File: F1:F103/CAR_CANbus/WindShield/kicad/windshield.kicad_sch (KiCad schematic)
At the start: 48 parts, among them J1 Screw_Terminal_01x02, J2 Screw_Terminal_01x02, J3 Screw_Terminal_01x02, Q1 IRLR7807, Q3 AOD4185, Q4 2N7002, Q5 2N7002, Q6 AOD4185, Q7 IRLR7807, U1 STM32F103C6Tx, U4 MT1470, U5 TJA1050, U6 XC6206PxxxMR, Y1 NX5032GA-8MHz

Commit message: continue of working on window
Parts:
- removed C1: 0.1, Capacitor_SMD:C_0603_1608Metric_Pad1.08x0.95mm_HandSolder, symbol Device:C
- removed C2: 2.2u/10u/47u, Capacitor_SMD:C_1206_3216Metric, symbol Device:C
- removed J1: Screw_Terminal_01x02, TerminalBlock_Phoenix:TerminalBlock_Phoenix_MKDS-1,5-2_1x02_P5.00mm_Horizontal, symbol Connector:Screw_Terminal_01x02
- added D1, D10, D12, D4, D7, D8: 1N4007, Diode_SMD:D_SMA_Handsoldering, symbol Device:D
- added D11, D13: MMZ3V3, Diode_SMD:D_SMA_Handsoldering, symbol Device:D_Schottky
- added D9: 1N5819, Diode_SMD:D_SOD-323_HandSoldering, symbol Device:D
- added J1: EXT_MOT, Connector_JST:JST_PH_B2B-PH-K_1x02_P2.00mm_Vertical, symbol Connector:Conn_01x02_Pin
- added J4: Power, symbol Connector:Screw_Terminal_01x03
- added J5: Hall, Connector_JST:JST_PH_B4B-PH-K_1x04_P2.00mm_Vertical, symbol Connector:Conn_01x04_Pin
- added J6: Buttons, Connector_JST:JST_PH_B3B-PH-K_1x03_P2.00mm_Vertical, symbol Connector:Conn_01x03_Pin
- added J7: UART, Connector_PinSocket_2.54mm:PinSocket_1x03_P2.54mm_Vertical, symbol Connector:Conn_01x03_Pin
- added J8: Prog, Connector_PinSocket_1.27mm:PinSocket_1x06_P1.27mm_Vertical, symbol Connector:Conn_01x06_Female
- added R18: 330, Resistor_SMD:R_0603_1608Metric_Pad0.98x0.95mm_HandSolder, symbol Device:R
- added R19: 47, Resistor_SMD:R_0603_1608Metric_Pad1.05x0.95mm_HandSolder, symbol Device:R
- added R20, R21, R22, R23: 100, Resistor_SMD:R_0603_1608Metric_Pad1.05x0.95mm_HandSolder, symbol Device:R
- added R24: 1k, Resistor_SMD:R_0603_1608Metric_Pad1.05x0.95mm_HandSolder, symbol Device:R
- added R25: 6.8, Resistor_SMD:R_0603_1608Metric_Pad0.98x0.95mm_HandSolder, symbol Device:R
- added R4: 0.05, Resistor_THT:R_Box_L14.0mm_W5.0mm_P9.00mm, symbol Device:R
- added R5, R6: 10k, Resistor_SMD:R_0603_1608Metric_Pad0.98x0.95mm_HandSolder, symbol Device:R
- added R7: 100, Resistor_SMD:R_0603_1608Metric_Pad0.98x0.95mm_HandSolder, symbol Device:R
- added TP1: L+, TestPoint:TestPoint_Loop_D1.80mm_Drill1.0mm_Beaded, symbol Connector:TestPoint
- added TP10, TP8, TP9: Gnd, TestPoint:TestPoint_Loop_D1.80mm_Drill1.0mm_Beaded, symbol Connector:TestPoint
- added TP11: 12V, TestPoint:TestPoint_Loop_D1.80mm_Drill1.0mm_Beaded, symbol Connector:TestPoint
- added TP2: L-, TestPoint:TestPoint_Loop_D1.80mm_Drill1.0mm_Beaded, symbol Connector:TestPoint
- added TP3, TP4: R-, TestPoint:TestPoint_Loop_D1.80mm_Drill1.0mm_Beaded, symbol Connector:TestPoint
- added TP5: Ven, TestPoint:TestPoint_Loop_D1.80mm_Drill1.0mm_Beaded, symbol Connector:TestPoint
- added TP6: 5V, TestPoint:TestPoint_Loop_D1.80mm_Drill1.0mm_Beaded, symbol Connector:TestPoint
- added TP7: 3V3, TestPoint:TestPoint_Loop_D1.80mm_Drill1.0mm_Beaded, symbol Connector:TestPoint
- added U2: ZXCT1009, Package_TO_SOT_SMD:SOT-23_Handsoldering, symbol ZXCT1009:ZXCT1009
- D5: footprint (none) -> Diode_SMD:D_SMB_Handsoldering
- J2: value Screw_Terminal_01x02 -> CAN; footprint TerminalBlock_Phoenix:TerminalBlock_Phoenix_MKDS-1,5-2_1x02_P5.00mm_Horizontal -> Connector_JST:JST_PH_B2B-PH-K_1x02_P2.00mm_Vertical; symbol Connector:Screw_Terminal_01x02 -> Connector:Conn_01x02_Pin
- JP1: footprint (none) -> Jumper:SolderJumper-2_P1.3mm_Open_TrianglePad1.0x1.5mm
- R1: value R -> 1k; footprint Resistor_SMD:R_0603_1608Metric_Pad0.98x0.95mm_HandSolder -> Resistor_SMD:R_0603_1608Metric_Pad1.05x0.95mm_HandSolder
- R12, R17: value 1k -> 10k
- U4: footprint (none) -> Package_TO_SOT_SMD:SOT-23-6_Handsoldering
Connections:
- net +12V: now also Q6.3 (S), D1.1 (K), D8.1 (K), J4.3 (Pin_3), R4.1, TP11.1, U2.2 (+); no longer Q3.2 (D), Q6.2 (D)
- net +3V3: now also C5.1, C6.1, C7.1, C8.1, U1.1 (VBAT), U1.24 (VDD), U1.36 (VDD), U1.48 (VDD), U1.9 (VDDA), D9.1 (K), R19.2, R25.1, TP7.1
- net +5V: now also TP6.1
- net CANH: now also J2.1 (Pin_1); no longer J2.2 (Pin_2)
- net CANL: now also J2.2 (Pin_2); no longer J2.1 (Pin_1)
- net GND: now also C5.2, C6.2, C7.2, C8.2, U1.23 (VSS), U1.35 (VSS), U1.47 (VSS), U1.8 (VSSA), D11.2 (A), D13.2 (A), D4.2 (A), D7.2 (A), J4.1 (Pin_1), J5.4 (Pin_4), J6.1 (Pin_1), J7.1 (Pin_1), J8.3 (Pin_3), R5.1, R6.2, R7.2, TP10.1, TP8.1, TP9.1
- net HOT@On: now also J4.2 (Pin_2)
- net L_DOWN: now also R5.2, TP2.1
- net L_UP: now also TP1.1
- net R_DOWN: now also R6.1, TP3.1
- net R_UP: now also TP4.1
- net VEN: now also TP5.1
- net at J3.1 (Pin_1), Q7.2 (D): now also Q6.2 (D), D1.2 (A), D4.1 (K); no longer Q6.3 (S)
- net at J3.2 (Pin_2), Q1.2 (D): now also Q3.2 (D), D7.1 (K), D8.2 (A); no longer Q3.3 (S)
- net UP_DIR: now reaches R1.1
- net UP_DIR: now also D11.1 (K)
- net at R1.2: now also D10.1 (K)
- new net: J6.3 (Pin_3), R23.1
- new net: Q3.3 (S), R4.2, U2.1 (-)
- new net: J5.1 (Pin_1), R19.1
- new net: J5.2 (Pin_2), R20.1
- new net: J5.3 (Pin_3), R21.1
- new net: R18.1, R7.1, U2.3 (sense)
- new net: J6.2 (Pin_2), R22.1
- new net: J8.4 (Pin_4), R25.2
- new net: D10.2 (A), J1.1 (Pin_1)
- new net: D12.2 (A), J1.2 (Pin_2)
- new net: D12.1 (K), R24.2
- new net BOOT0: J8.5 (Pin_5)
- new net DOWN_BTN: R22.2
- new net DOWN_DIR: D13.1 (K), R24.1
- new net DOWN_SW: R21.2
- new net NRST: J8.6 (Pin_6)
- new net Rx: J7.2 (Pin_2)
- new net SWCLK: J8.1 (Pin_1)
- new net SWDIO: J8.2 (Pin_2)
- new net Tx: J7.3 (Pin_3)
- new net UP_BTN: R23.2
- new net UP_SW: R20.2
- new net Vsen: D9.2 (A), R18.2
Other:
- note added: "5W"
- note added: "Connect motor so that (2) of J3 is positive when window goes up!!!"
- note added: "Control by car windows manage system"
- note added: "Control by simplest buttons"
- note added: "Hall sensors"
- note added: "Power"
- note added: "Program & configure"
- note removed: "HALL A/B"
- moved on the sheet: C11, C12, C13, C14, C16, C17, C5, C6, C7, C8, D2, D6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

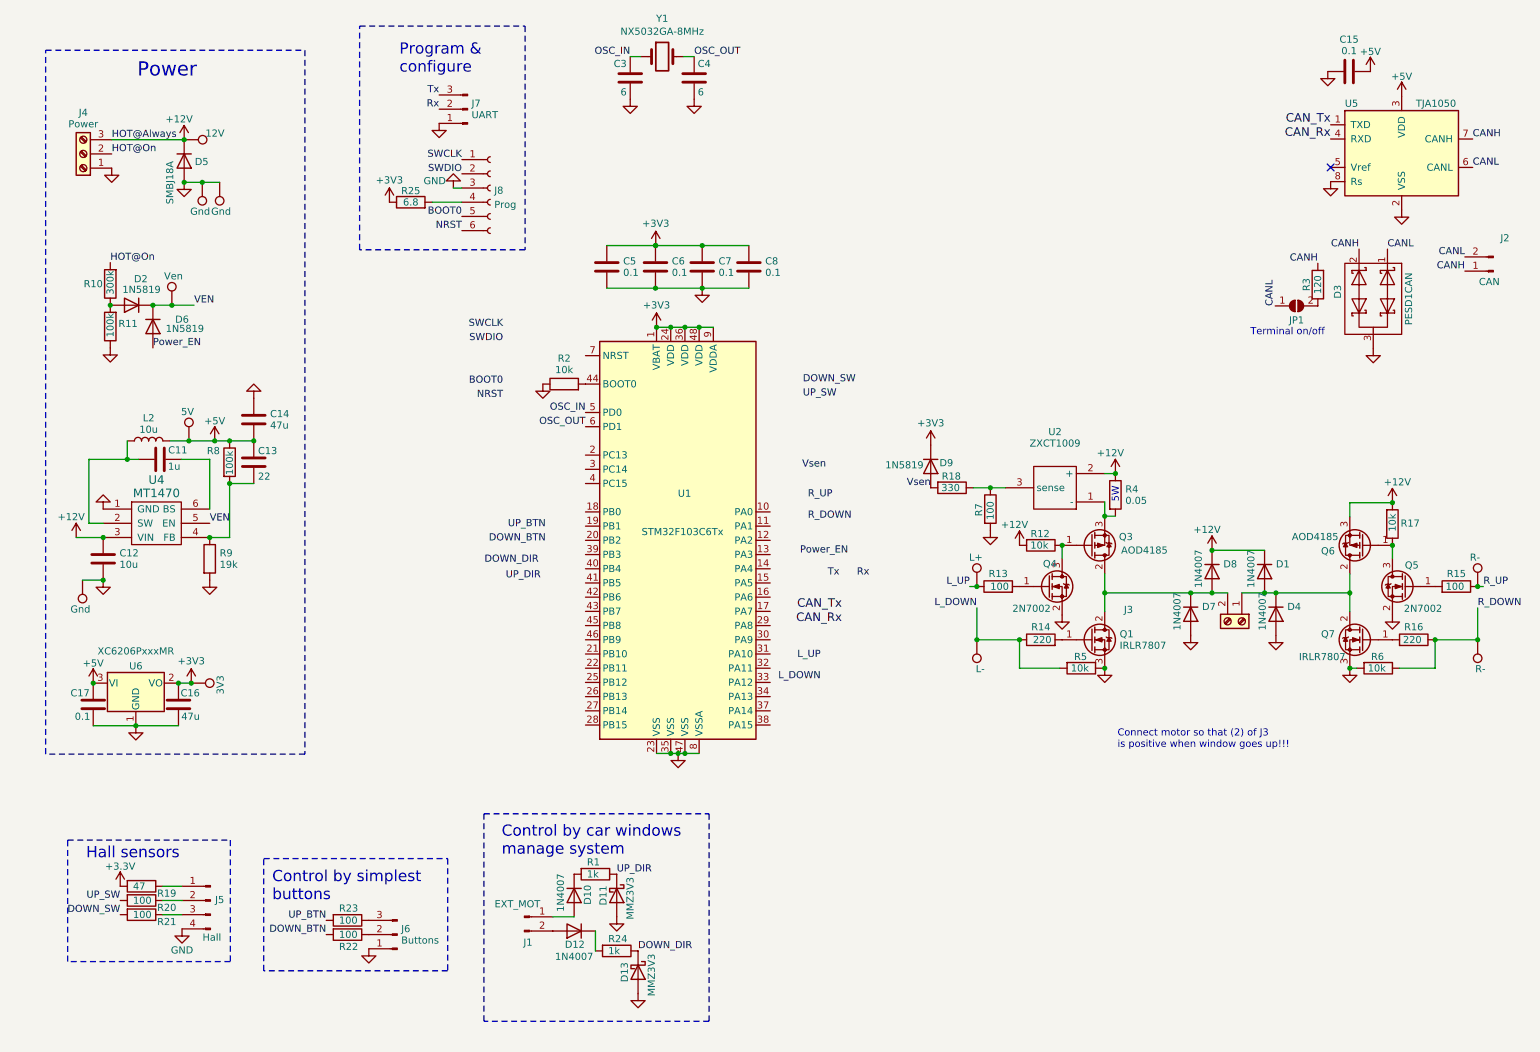
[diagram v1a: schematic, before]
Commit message: start drawing a PCB
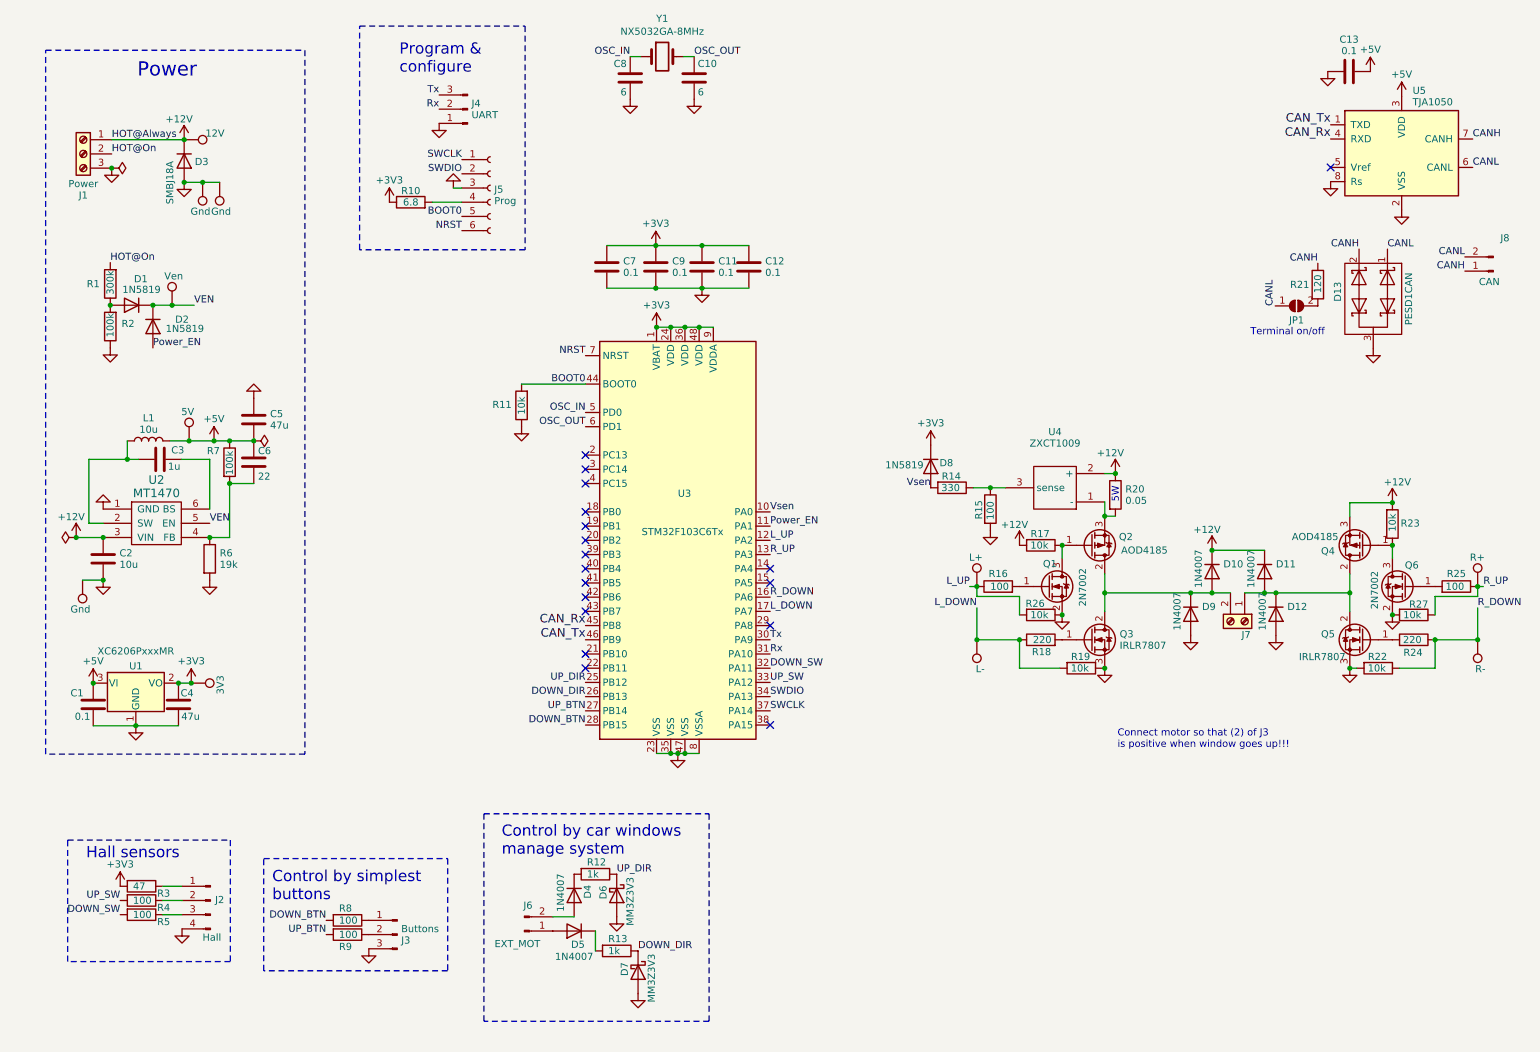
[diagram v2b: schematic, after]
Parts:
- removed R3: 120, Resistor_SMD:R_1210_3225Metric_Pad1.42x2.65mm_HandSolder, symbol stm32-rescue:R
- removed U5: TJA1050, Package_SO:SOIC-8_3.9x4.9mm_P1.27mm, symbol stm32-rescue:MCP2551-I_SN
- added R21: 120, Resistor_SMD:R_1210_3225Metric_Pad1.30x2.65mm_HandSolder, symbol Device:R
- added R26, R27: 10k, Resistor_SMD:R_0603_1608Metric_Pad0.98x0.95mm_HandSolder, symbol Device:R
- added U5: TJA1050, Package_SO:SOIC-8_3.9x4.9mm_P1.27mm, symbol Interface_CAN_LIN:MCP2551-I-SN
- D6: renamed from D11; value MMZ3V3 -> MM3Z3V3; footprint Diode_SMD:D_SMA_Handsoldering -> Diode_SMD:D_0805_2012Metric_Pad1.15x1.40mm_HandSolder
- D7: renamed from D13; value MMZ3V3 -> MM3Z3V3; footprint Diode_SMD:D_SMA_Handsoldering -> Diode_SMD:D_0805_2012Metric_Pad1.15x1.40mm_HandSolder
- J1: renamed from J4; footprint (none) -> TerminalBlock_Phoenix:TerminalBlock_Phoenix_MKDS-1,5-3-5.08_1x03_P5.08mm_Horizontal
- J5: renamed from J8; symbol Connector:Conn_01x06_Female -> Connector:Conn_01x06_Socket
- R12: renamed from R1; footprint Resistor_SMD:R_0603_1608Metric_Pad1.05x0.95mm_HandSolder -> Resistor_SMD:R_0603_1608Metric_Pad0.98x0.95mm_HandSolder
- R13: renamed from R24; footprint Resistor_SMD:R_0603_1608Metric_Pad1.05x0.95mm_HandSolder -> Resistor_SMD:R_0603_1608Metric_Pad0.98x0.95mm_HandSolder
- R3: renamed from R19; footprint Resistor_SMD:R_0603_1608Metric_Pad1.05x0.95mm_HandSolder -> Resistor_SMD:R_0603_1608Metric_Pad0.98x0.95mm_HandSolder
- R4: renamed from R20; footprint Resistor_SMD:R_0603_1608Metric_Pad1.05x0.95mm_HandSolder -> Resistor_SMD:R_0603_1608Metric_Pad0.98x0.95mm_HandSolder
- R5: renamed from R21; footprint Resistor_SMD:R_0603_1608Metric_Pad1.05x0.95mm_HandSolder -> Resistor_SMD:R_0603_1608Metric_Pad0.98x0.95mm_HandSolder
- R8: renamed from R23; footprint Resistor_SMD:R_0603_1608Metric_Pad1.05x0.95mm_HandSolder -> Resistor_SMD:R_0603_1608Metric_Pad0.98x0.95mm_HandSolder
- R9: renamed from R22; footprint Resistor_SMD:R_0603_1608Metric_Pad1.05x0.95mm_HandSolder -> Resistor_SMD:R_0603_1608Metric_Pad0.98x0.95mm_HandSolder
- TP10: renamed from TP4; value R- -> R+
- renumbered C17 to C1, C4 to C10, C7 to C11, C8 to C12, C15 to C13, C12 to C2, C11 to C3, C16 to C4, C14 to C5, C13 to C6, C5 to C7, C3 to C8, C6 to C9, D2 to D1, D8 to D10, D1 to D11, D4 to D12, D3 to D13, D6 to D2, D5 to D3, D10 to D4, D12 to D5, D9 to D8, D7 to D9, J5 to J2, J6 to J3, J7 to J4, J1 to J6, J3 to J7, J2 to J8, L2 to L1, Q4 to Q1, Q3 to Q2, Q1 to Q3, Q6 to Q4, Q7 to Q5, Q5 to Q6, R10 to R1, R25 to R10, R2 to R11, R18 to R14, R7 to R15, R13 to R16, R12 to R17, R14 to R18, R5 to R19, R11 to R2, R4 to R20, R6 to R22, R17 to R23, R16 to R24, R15 to R25, R9 to R6, R8 to R7, TP8 to TP1, TP3 to TP11, TP5 to TP2, TP11 to TP3, TP6 to TP4, TP7 to TP5, TP10 to TP6, TP9 to TP7, TP1 to TP8, TP2 to TP9, U6 to U1, U4 to U2, U1 to U3, U2 to U4
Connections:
- net +12V: now also J1.1 (Pin_1); no longer J1.3 (Pin_3)
- net +5V: now also U5.3 (VDD)
- net BOOT0: now also R11.2, U3.44 (BOOT0)
- net CANH: now also R21.1, U5.7 (CANH)
- net CANL: now also U5.6 (CANL)
- net CAN_Rx: now also U3.45 (PB8), U5.4 (RXD)
- net CAN_Tx: now also U3.46 (PB9), U5.1 (TXD)
- net DOWN_BTN: now also R8.2, U3.28 (PB15); no longer R9.2
- net DOWN_DIR: now also U3.26 (PB13)
- net DOWN_SW: now also U3.32 (PA11)
- net GND: now also J1.3 (Pin_3), J3.3 (Pin_3), R26.1, R27.2, U5.2 (VSS), U5.8 (Rs); no longer J1.1 (Pin_1), J3.1 (Pin_1)
- net L_DOWN: now also U3.17 (PA7)
- net L_UP: now also U3.12 (PA2), R26.2
- net NRST: now also U3.7 (NRST)
- net Power_EN: now also U3.11 (PA1)
- net R_DOWN: now also U3.16 (PA6)
- net R_UP: now also U3.13 (PA3), R27.1
- net Rx: now also U3.31 (PA10)
- net SWCLK: now also U3.37 (PA14)
- net SWDIO: now also U3.34 (PA13)
- net Tx: now also U3.30 (PA9)
- net UP_BTN: now also R9.2, U3.27 (PB14); no longer R8.2
- net UP_DIR: now also U3.25 (PB12)
- net UP_SW: now also U3.33 (PA12)
- net Vsen: now also U3.10 (PA0)
- net at R8.1: now also J3.1 (Pin_1); no longer J3.3 (Pin_3)
- net at JP1.2 (B): now also R21.2
- net at J6.1 (Pin_1): now also D5.2 (A); no longer D4.2 (A)
- net at J6.2 (Pin_2): now also D4.2 (A); no longer D5.2 (A)
- no-connect marks 1 -> 18
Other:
- moved on the sheet: J1, J3, J7, R11

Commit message: finished PCB
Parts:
- J7: value Screw_Terminal_01x02 -> Motor
- JP1: value SolderJumper_2_Open -> Term
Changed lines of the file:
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@@
       (effects (font (size 1.27 1.27)))
     )
-    (property "Value" "SolderJumper_2_Open" (at 244.348 62.095 0)
+    (property "Value" "Term" (at 244.348 62.095 0)
       (effects (font (size 1.27 1.27)) hide)
     )
@@
       (effects (font (size 1.27 1.27)))
     )
-    (property "Value" "Screw_Terminal_01x02" (at 232.5624 122.936 0)
+    (property "Value" "Motor" (at 232.5624 122.936 0)
       (effects (font (size 1.27 1.27)) (justify left) hide)
     )

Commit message: add buttons, not tested yet
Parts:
- removed D4, D5: 1N4007, Diode_SMD:D_SMA_Handsoldering, symbol Device:D
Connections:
- net +12V: no longer Q4.3 (S), R23.2
- net at Q2.3 (S), R20.2, U4.1 (-): now also Q4.3 (S), R23.2
- net at J6.1 (Pin_1): now also R13.2
- net at J6.2 (Pin_2): now also R12.2
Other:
- note added: "Заменить на HC-49"
